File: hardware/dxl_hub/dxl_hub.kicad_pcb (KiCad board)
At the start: 2 copper layers, 22.3 x 28.2 mm, 12 parts, among them CN1 B3B-EH-A (LF)(SN), CN2 A2007WR-3P, CN3 B3B-EH-A (LF)(SN), CN4 A2007WR-3P, CN5 B3B-EH-A (LF)(SN), CN6 B3B-PH-K-S(LF)(SN), CN7 B3B-EH-A (LF)(SN), CN8 B3B-PH-K-S(LF)(SN), J1 1.8mm螺丝孔, J2 1.8mm螺丝孔

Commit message: update: BOM
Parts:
- C1: value cape -> 1000uF/10V固态
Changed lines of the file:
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@@
 			)
 		)
-		(property "Value" "cape"
+		(property "Value" "1000uF/10V固态"
 			(at 0.0381 4.9666 90)
 			(layer "F.Fab")

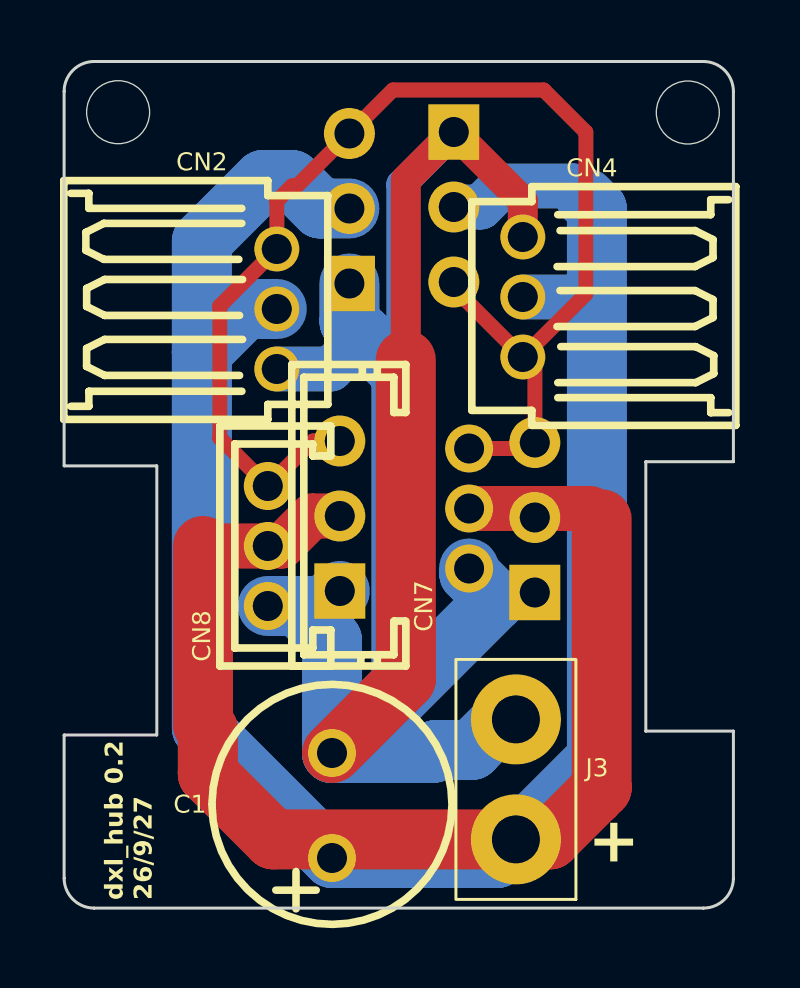
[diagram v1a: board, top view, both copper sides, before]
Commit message: hardware:升级dxl_hub。左右腿飞特舵机线移动到背面，解决与脖子舵机略微干涉放不到底的问题
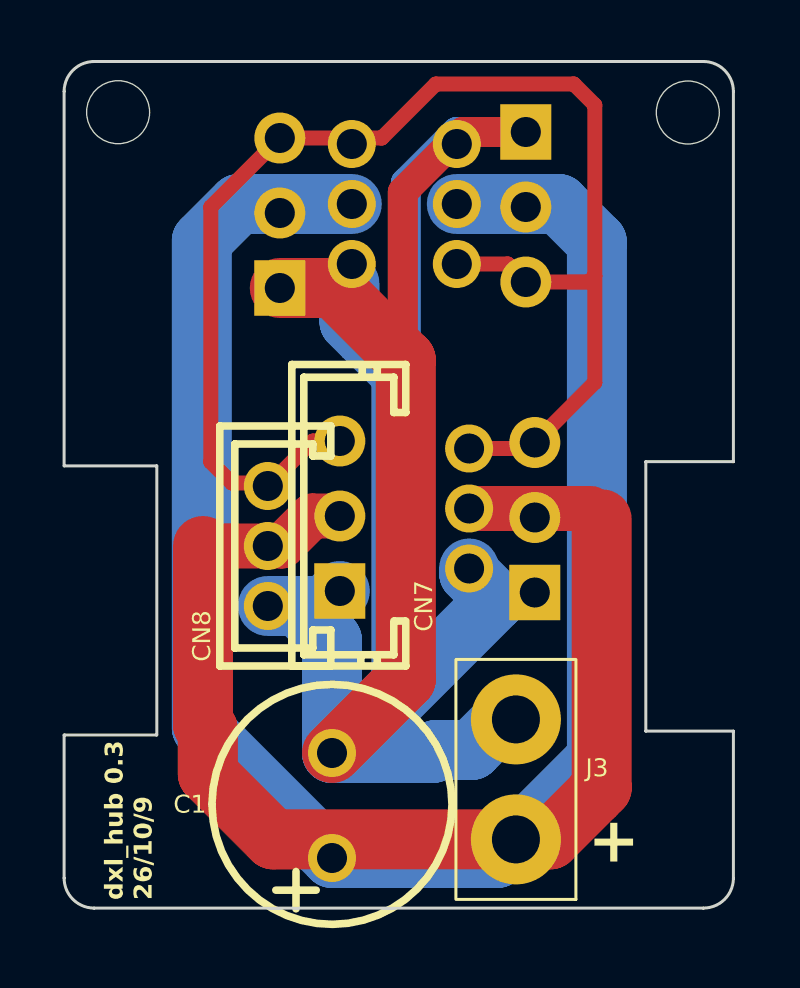
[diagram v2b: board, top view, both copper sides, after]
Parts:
- CN2, CN4: value A2007WR-3P -> B3B-PH-K-S(LF)(SN); footprint microduck:CONN-TH_A2007WR-3P -> microduck:CONN-TH_B3B-PH-K-S; moved to B.Cu
- moved CN2 6.95 mm to (141.9, 82.0), turned to -90 degrees
- moved CN4 6.49 mm to (138.4, 82.0), turned to 90 degrees
- moved CN1 2.40 mm to (144.2, 82.1)
- moved CN3 2.32 mm to (136.0, 82.3)
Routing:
- net +BATT: track 108.9 -> 101.4 mm
- net /DATA: track 43.5 -> 47.8 mm
- net GND: track 79.6 -> 81.6 mm
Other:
- board text added: "dxl_hub 0.3 26/10/9"
- board text removed: "dxl_hub 0.2 26/9/27"
